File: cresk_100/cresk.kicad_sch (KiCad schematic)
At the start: 52 parts, among them J1 8P8C, J2 8P8C, J3 Conn_01x05_Male, J4 Conn_01x05_Male, SW1 SW_Push, SW10 SW_Push, SW11 SW_Push, SW12 SW_Push, SW13 SW_Push, SW14 SW_Push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

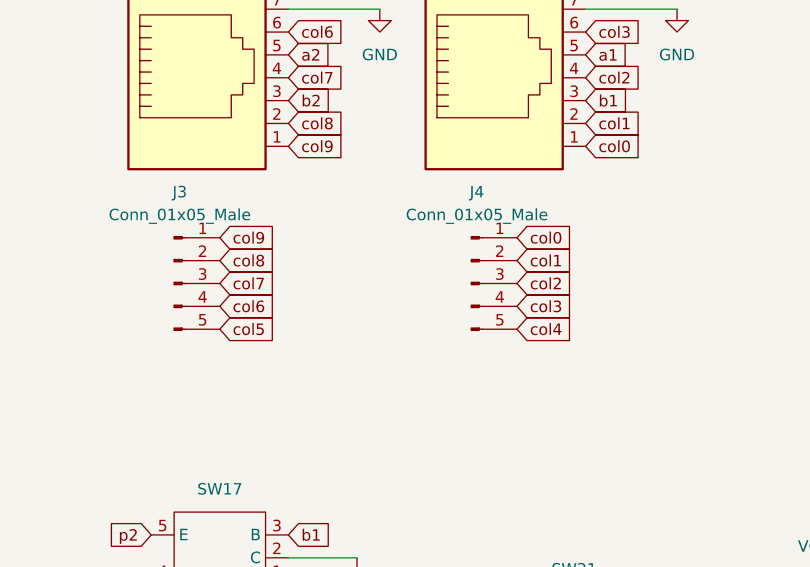
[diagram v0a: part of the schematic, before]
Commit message: cresk_100: update through hole size
Pad size to 1.6 mm and drill to 1 mm.
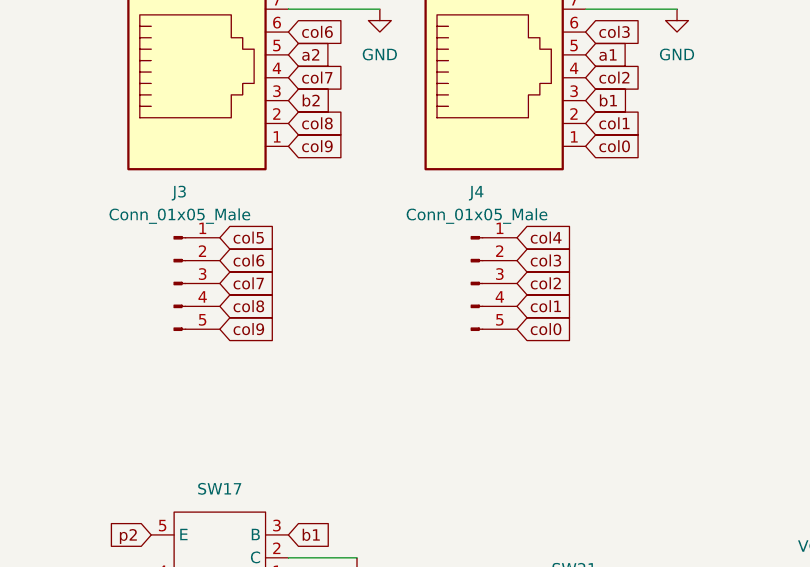
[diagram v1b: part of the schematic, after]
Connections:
- net col0: now also J4.5 (Pin_5); no longer J4.1 (Pin_1)
- net col1: now also J4.4 (Pin_4); no longer J4.2 (Pin_2)
- net col3: now also J4.2 (Pin_2); no longer J4.4 (Pin_4)
- net col4: now also J4.1 (Pin_1); no longer J4.5 (Pin_5)
- net col5: now also J3.1 (Pin_1); no longer J3.5 (Pin_5)
- net col6: now also J3.2 (Pin_2); no longer J3.4 (Pin_4)
- net col8: now also J3.4 (Pin_4); no longer J3.2 (Pin_2)
- net col9: now also J3.5 (Pin_5); no longer J3.1 (Pin_1)
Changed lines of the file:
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@@
     )
   )
-  (global_label "col0" (shape input) (at 223.52 55.88 0) (fields_autoplaced)
-    (effects (font (size 1.27 1.27)) (justify left))
-    (property "Intersheet References" "${INTERSHEET_REFS}" (id 0) (at 230.0455 55.8006 0)
+  (global_label "col0" (shape input) (at 223.52 66.04 0) (fields_autoplaced)
+    (effects (font (size 1.27 1.27)) (justify left))
+    (property "Intersheet References" "${INTERSHEET_REFS}" (id 0) (at 230.0455 66.1194 0)
       (effects (font (size 1.27 1.27)) (justify left) hide)
     )
@@
     )
   )
-  (global_label "col1" (shape input) (at 223.52 58.42 0) (fields_autoplaced)
-    (effects (font (size 1.27 1.27)) (justify left))
-    (property "Intersheet References" "${INTERSHEET_REFS}" (id 0) (at 230.0455 58.3406 0)
+  (global_label "col1" (shape input) (at 223.52 63.5 0) (fields_autoplaced)
+    (effects (font (size 1.27 1.27)) (justify left))
+    (property "Intersheet References" "${INTERSHEET_REFS}" (id 0) (at 230.0455 63.5794 0)
       (effects (font (size 1.27 1.27)) (justify left) hide)
     )
@@
     )
   )
-  (global_label "col8" (shape input) (at 190.5 58.42 0) (fields_autoplaced)
-    (effects (font (size 1.27 1.27)) (justify left))
-    (property "Intersheet References" "${INTERSHEET_REFS}" (id 0) (at 197.0255 58.4994 0)
+  (global_label "col8" (shape input) (at 190.5 63.5 0) (fields_autoplaced)
+    (effects (font (size 1.27 1.27)) (justify left))
+    (property "Intersheet References" "${INTERSHEET_REFS}" (id 0) (at 197.0255 63.4206 0)
       (effects (font (size 1.27 1.27)) (justify left) hide)
     )
@@
     )
   )
-  (global_label "col3" (shape input) (at 223.52 63.5 0) (fields_autoplaced)
-    (effects (font (size 1.27 1.27)) (justify left))
-    (property "Intersheet References" "${INTERSHEET_REFS}" (id 0) (at 230.0455 63.4206 0)
+  (global_label "col3" (shape input) (at 223.52 58.42 0) (fields_autoplaced)
+    (effects (font (size 1.27 1.27)) (justify left))
+    (property "Intersheet References" "${INTERSHEET_REFS}" (id 0) (at 230.0455 58.4994 0)
       (effects (font (size 1.27 1.27)) (justify left) hide)
     )
@@
     )
   )
-  (global_label "col4" (shape input) (at 223.52 66.04 0) (fields_autoplaced)
-    (effects (font (size 1.27 1.27)) (justify left))
-    (property "Intersheet References" "${INTERSHEET_REFS}" (id 0) (at 230.0455 65.9606 0)
-      (effects (font (size 1.27 1.27)) (justify left) hide)
-    )
-  )
-  (global_label "col6" (shape input) (at 190.5 63.5 0) (fields_autoplaced)
-    (effects (font (size 1.27 1.27)) (justify left))
-    (property "Intersheet References" "${INTERSHEET_REFS}" (id 0) (at 197.0255 63.5794 0)
+  (global_label "col4" (shape input) (at 223.52 55.88 0) (fields_autoplaced)
+    (effects (font (size 1.27 1.27)) (justify left))
+    (property "Intersheet References" "${INTERSHEET_REFS}" (id 0) (at 230.0455 55.9594 0)
+      (effects (font (size 1.27 1.27)) (justify left) hide)
+    )
+  )
+  (global_label "col6" (shape input) (at 190.5 58.42 0) (fields_autoplaced)
+    (effects (font (size 1.27 1.27)) (justify left))
+    (property "Intersheet References" "${INTERSHEET_REFS}" (id 0) (at 197.0255 58.3406 0)
       (effects (font (size 1.27 1.27)) (justify left) hide)
     )
@@
     )
   )
-  (global_label "col5" (shape input) (at 190.5 66.04 0) (fields_autoplaced)
-    (effects (font (size 1.27 1.27)) (justify left))
-    (property "Intersheet References" "${INTERSHEET_REFS}" (id 0) (at 197.0255 66.1194 0)
+  (global_label "col5" (shape input) (at 190.5 55.88 0) (fields_autoplaced)
+    (effects (font (size 1.27 1.27)) (justify left))
+    (property "Intersheet References" "${INTERSHEET_REFS}" (id 0) (at 197.0255 55.8006 0)
       (effects (font (size 1.27 1.27)) (justify left) hide)
     )
@@
     )
   )
-  (global_label "col9" (shape input) (at 190.5 55.88 0) (fields_autoplaced)
-    (effects (font (size 1.27 1.27)) (justify left))
-    (property "Intersheet References" "${INTERSHEET_REFS}" (id 0) (at 197.0255 55.9594 0)
+  (global_label "col9" (shape input) (at 190.5 66.04 0) (fields_autoplaced)
+    (effects (font (size 1.27 1.27)) (justify left))
+    (property "Intersheet References" "${INTERSHEET_REFS}" (id 0) (at 197.0255 65.9606 0)
       (effects (font (size 1.27 1.27)) (justify left) hide)
     )
@@
   (global_label "col7" (shape input) (at 190.5 60.96 0) (fields_autoplaced)
     (effects (font (size 1.27 1.27)) (justify left))
-    (property "Intersheet References" "${INTERSHEET_REFS}" (id 0) (at 197.0255 61.0394 0)
+    (property "Intersheet References" "${INTERSHEET_REFS}" (id 0) (at 197.0255 60.8806 0)
       (effects (font (size 1.27 1.27)) (justify left) hide)
     )
@@
   (global_label "col2" (shape input) (at 223.52 60.96 0) (fields_autoplaced)
     (effects (font (size 1.27 1.27)) (justify left))
-    (property "Intersheet References" "${INTERSHEET_REFS}" (id 0) (at 230.0455 60.8806 0)
-      (effects (font (size 1.27 1.27)) (justify left) hide)
-    )
+    (property "Intersheet References" "${INTERSHEET_REFS}" (id 0) (at 230.0455 61.0394 0)
+      (effects (font (size 1.27 1.27)) (justify left) hide)
+    )

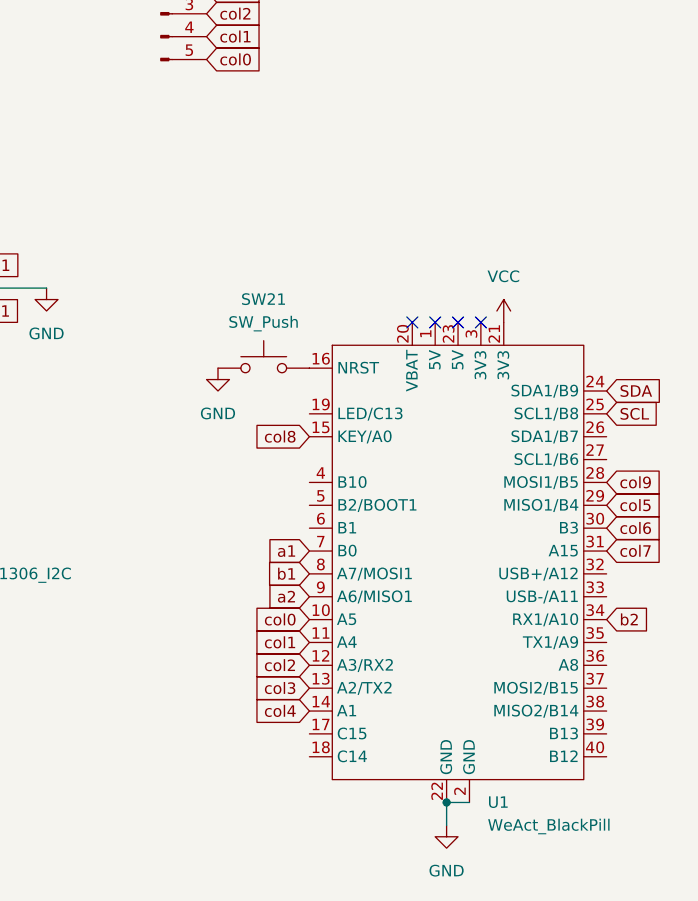
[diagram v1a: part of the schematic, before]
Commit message: cresk_100: change pin mapping
Make it compatible with non flipped BlackPill, and possibly ProMicro.
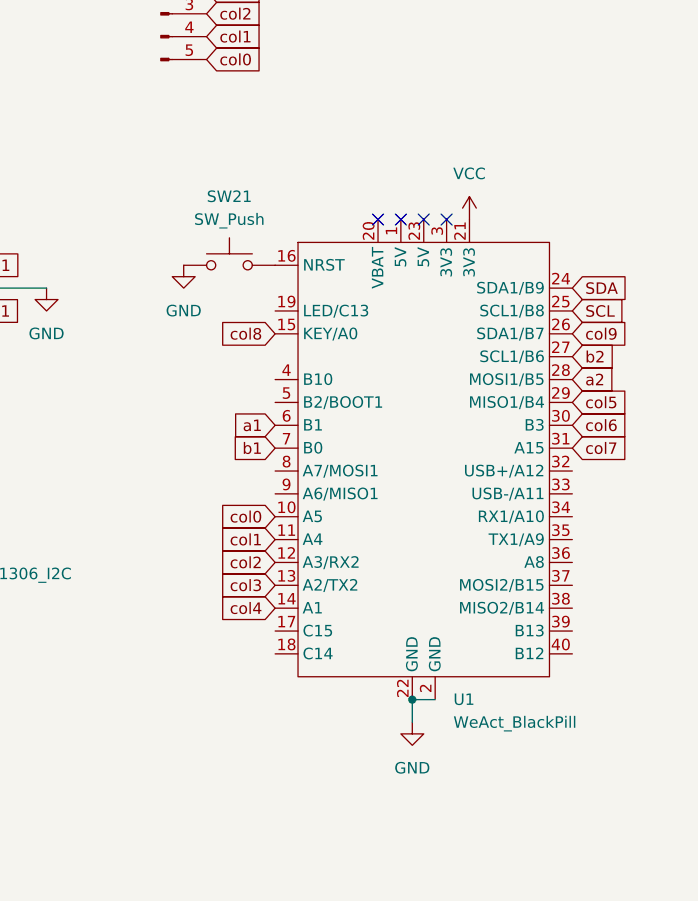
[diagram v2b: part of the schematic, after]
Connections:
- net a1: now also U1.6 (B1); no longer U1.7 (B0)
- net a2: now also U1.28 (MOSI1/B5); no longer U1.9 (A6/MISO1)
- net b1: now also U1.7 (B0); no longer U1.8 (A7/MOSI1)
- net b2: now also U1.27 (SCL1/B6); no longer U1.34 (RX1/A10)
- net col9: now also U1.26 (SDA1/B7); no longer U1.28 (MOSI1/B5)
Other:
- moved on the sheet: SW21, U1
